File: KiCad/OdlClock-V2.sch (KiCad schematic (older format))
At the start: 25 parts

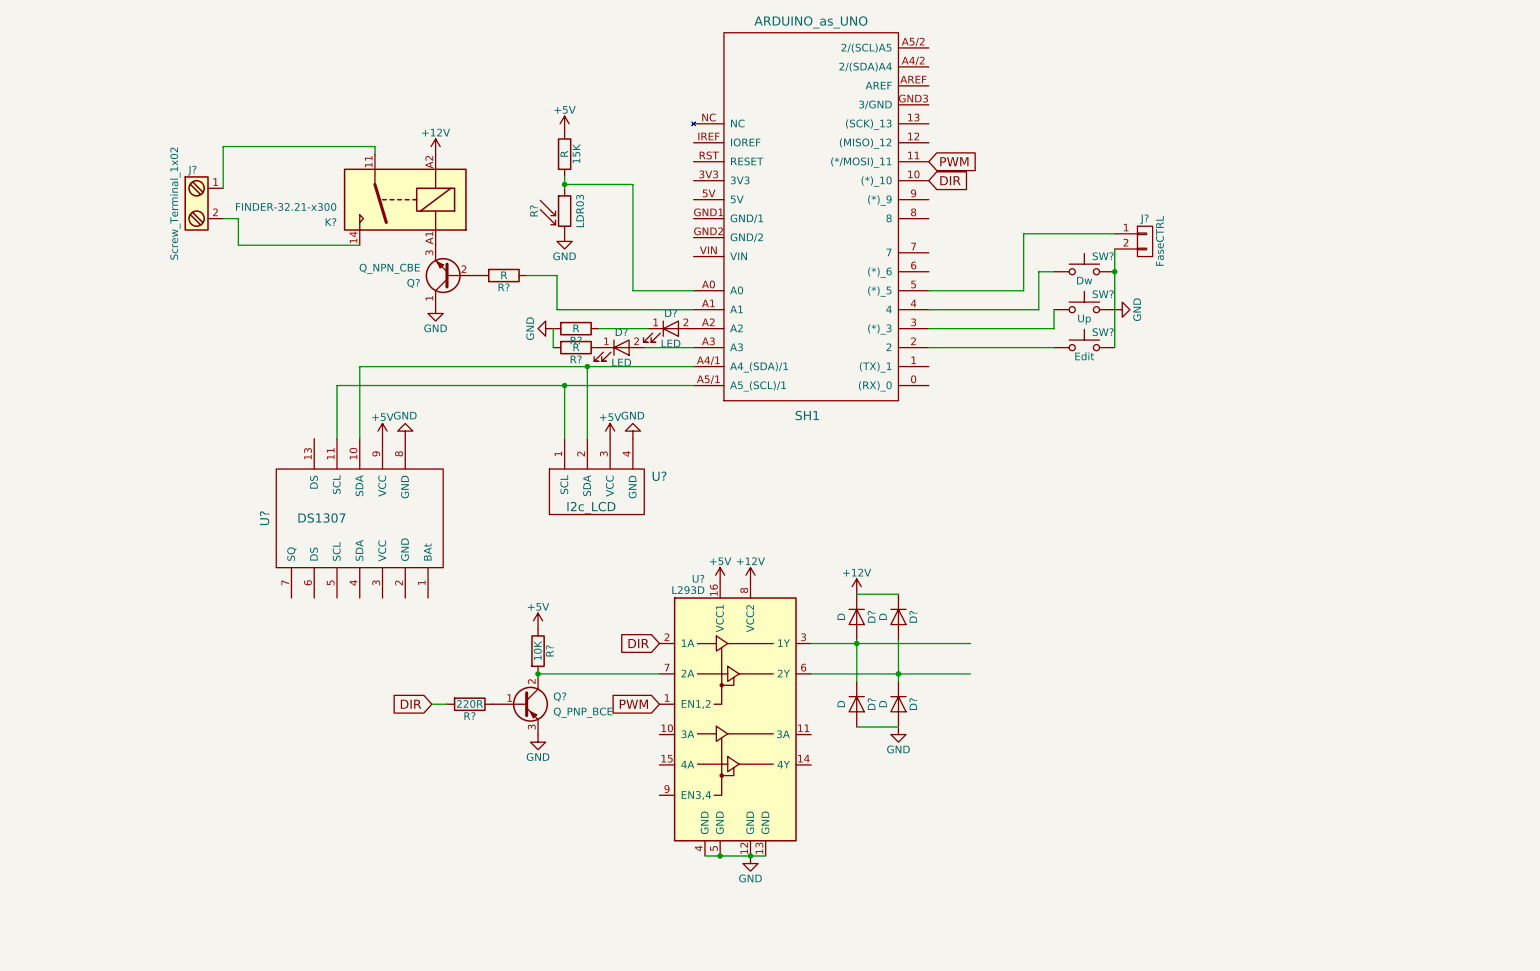
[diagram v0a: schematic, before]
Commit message: Modified SCH Enable and Dir pin to avoid motor revolution during the USB reset
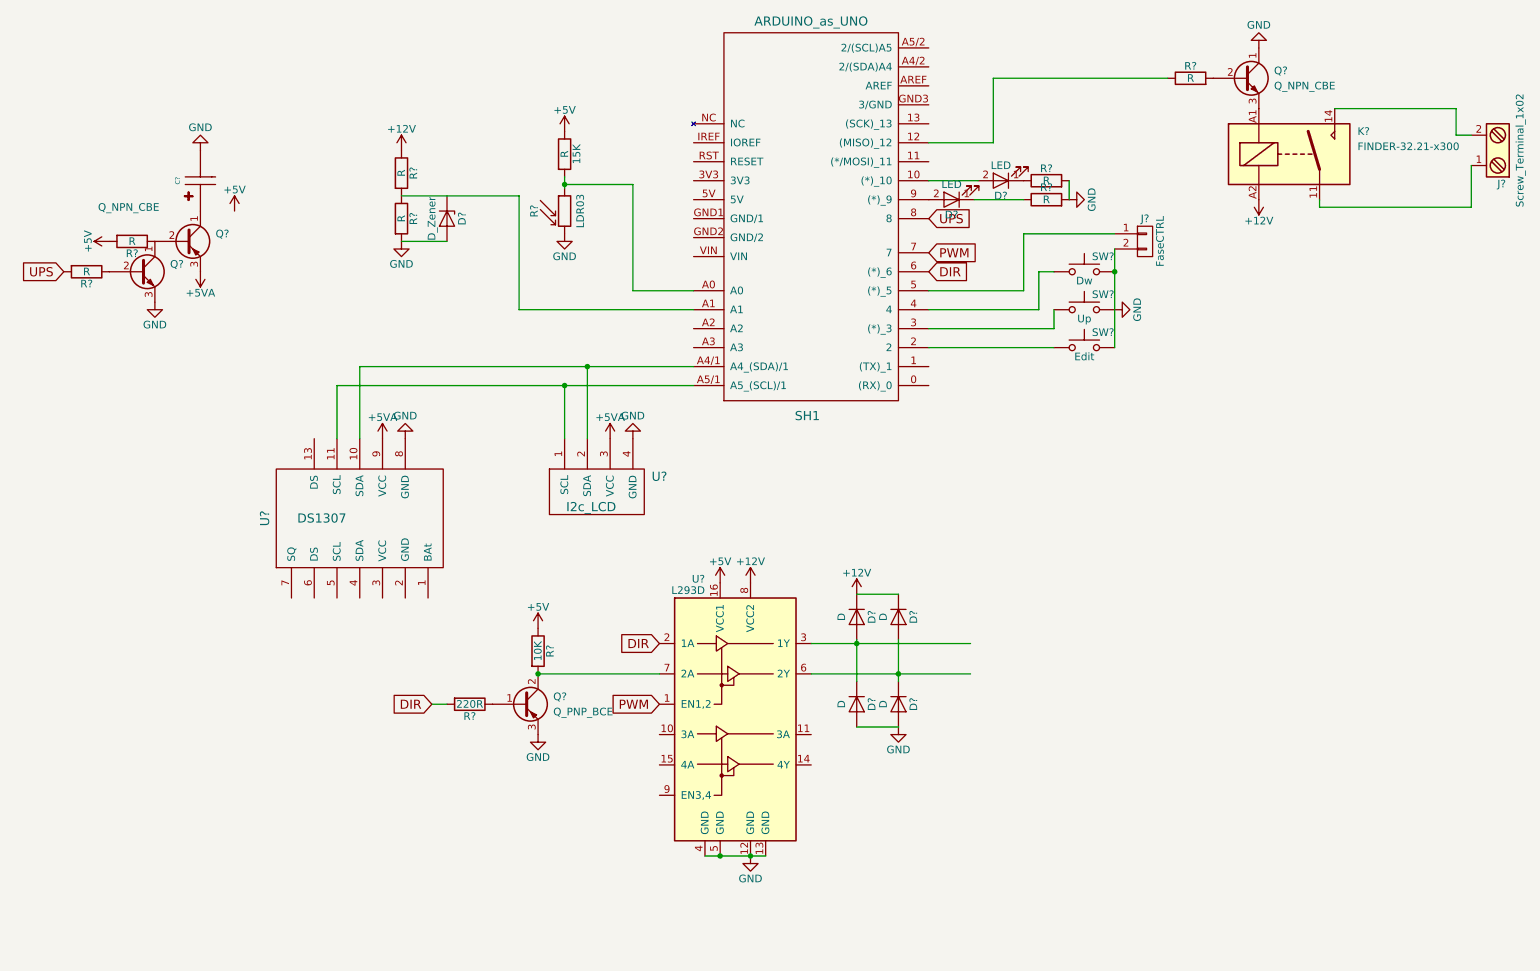
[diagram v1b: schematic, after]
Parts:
- added C?: CAPACITOR_POLARISED_RevE_Date15jun2010, symbol CAPACITOR_POLARISED_RevE_Date15jun2010
- added D?: D_Zener, symbol D_Zener
- added Q?: Q_PNP_CBE, symbol Q_PNP_CBE
- added Q?: Q_NPN_CBE, symbol Q_NPN_CBE
- added R? (x4): R, symbol R
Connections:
- net labels added: +5VA, UPS
- wire segments 41 -> 45
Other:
- moved on the sheet: D?, J?, K?, Q?, R?

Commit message: Step Down regulator Q
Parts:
- added C2: 470uF 25V, symbol CAPACITOR_POLARISED_RevE_Date15jun2010
- added C3: 220nf, symbol C
- added D1: BA159, symbol DIODE-STANDARD_RevE_Date15jun2010
- added J3, J4: Screw_Terminal_1x02, symbol Screw_Terminal_1x02
- added L1: L, symbol L
- added U1: LM2575-5.0BT, TO_SOT_Packages_THT:TO-220-5_Vertical, symbol LM2575-5.0BT
- D3, D4, D5, D6: renamed from D?; value D -> BA159
- gave numbers to parts that had none: 27
- renumbered 15K to 15K1
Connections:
- wire segments 45 -> 52
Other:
- moved on the sheet: C1
